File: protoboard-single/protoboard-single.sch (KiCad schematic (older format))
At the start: 1 part, among them J1 MODULE_HEADER

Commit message: mvp
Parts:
- added J10, J11, J12, J13, J14, J2, J3, J4, J5, J6, J7, J8, J9: MODULE_HEADER, parts:1x10, symbol MODULE_HEADER
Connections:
- net at J1.1 (GND): now also J14.1 (GND)
- net at J1.10 (G3): now also J14.10 (G3)
- net at J1.2 (3V3): now also J14.2 (3V3)
- net at J1.3 (SCL): now also J14.3 (SCL)
- net at J1.4 (SDA): now also J14.4 (SDA)
- net at J1.5 (CLK): now also J14.5 (CLK)
- net at J1.6 (MISO): now also J14.6 (MISO)
- net at J1.7 (MOSI): now also J14.7 (MOSI)
- net at J1.8 (G1/TX): now also J14.8 (G1/TX)
- net at J1.9 (G2/RX): now also J14.9 (G2/RX)
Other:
- note added: "cheating to get some through holes"
- moved on the sheet: J1
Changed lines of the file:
@@
 LIBS:valves
 LIBS:parts
-LIBS:protoboard-single-cache
 EELAYER 24 0
 EELAYER END
@@
 L MODULE_HEADER J1
 U 1 1 540E6C30
-P 5950 4000
-F 0 "J1" H 5600 4550 60  0000 C CNN
-F 1 "MODULE_HEADER" V 5650 3950 60  0000 C CNN
-F 2 "parts:MODULE_HEADER_MODULE" H 5950 4000 60  0001 C CNN
-F 3 "" H 5950 4000 60  0000 C CNN
-	1    5950 4000
+P 5400 2800
+F 0 "J1" H 5050 3350 60  0000 C CNN
+F 1 "MODULE_HEADER" V 5100 2750 60  0000 C CNN
+F 2 "parts:MODULE_HEADER_MODULE" H 5400 2800 60  0001 C CNN
+F 3 "" H 5400 2800 60  0000 C CNN
+	1    5400 2800
 	1    0    0    -1
 $EndComp
+$Comp
+L MODULE_HEADER J5
+U 1 1 540E71D1
+P 3450 5750
+F 0 "J5" H 3100 6300 60  0000 C CNN
+F 1 "MODULE_HEADER" V 3150 5700 60  0000 C CNN
+F 2 "parts:1x10" H 3450 5750 60  0001 C CNN
+F 3 "" H 3450 5750 60  0000 C CNN
+	1    3450 5750
+	1    0    0    -1
+$EndComp
+$Comp
+L MODULE_HEADER J6
+U 1 1 540E7221
+P 4300 5750
+F 0 "J6" H 3950 6300 60  0000 C CNN
+F 1 "MODULE_HEADER" V 4000 5700 60  0000 C CNN
+F 2 "parts:1x10" H 4300 5750 60  0001 C CNN
+F 3 "" H 4300 5750 60  0000 C CNN
+	1    4300 5750
+	1    0    0    -1
+$EndComp
+$Comp
+L MODULE_HEADER J7
+U 1 1 540E72AE
+P 5150 5750
+F 0 "J7" H 4800 6300 60  0000 C CNN
+F 1 "MODULE_HEADER" V 4850 5700 60  0000 C CNN
+F 2 "parts:1x10" H 5150 5750 60  0001 C CNN
+F 3 "" H 5150 5750 60  0000 C CNN
+	1    5150 5750
+	1    0    0    -1
+$EndComp
+$Comp
+L MODULE_HEADER J8
+U 1 1 540E72B4
+P 6000 5750
+F 0 "J8" H 5650 6300 60  0000 C CNN
+F 1 "MODULE_HEADER" V 5700 5700 60  0000 C CNN
+F 2 "parts:1x10" H 6000 5750 60  0001 C CNN
+F 3 "" H 6000 5750 60  0000 C CNN
+	1    6000 5750
+	1    0    0    -1
+$EndComp
+$Comp
+L MODULE_HEADER J9
+U 1 1 540E746F
+P 6850 5750
+F 0 "J9" H 6500 6300 60  0000 C CNN
+F 1 "MODULE_HEADER" V 6550 5700 60  0000 C CNN
+F 2 "parts:1x10" H 6850 5750 60  0001 C CNN
+F 3 "" H 6850 5750 60  0000 C CNN
+	1    6850 5750
+	1    0    0    -1
+$EndComp
+$Comp
+L MODULE_HEADER J10
+U 1 1 540E7475
+P 7700 5750
+F 0 "J10" H 7350 6300 60  0000 C CNN
+F 1 "MODULE_HEADER" V 7400 5700 60  0000 C CNN
+F 2 "parts:1x10" H 7700 5750 60  0001 C CNN
+F 3 "" H 7700 5750 60  0000 C CNN
+	1    7700 5750
+	1    0    0    -1
+$EndComp
+$Comp
+L MODULE_HEADER J11
+U 1 1 540E747B
+P 8550 5750
+F 0 "J11" H 8200 6300 60  0000 C CNN
+F 1 "MODULE_HEADER" V 8250 5700 60  0000 C CNN
+F 2 "parts:1x10" H 8550 5750 60  0001 C CNN
+F 3 "" H 8550 5750 60  0000 C CNN
+	1    8550 5750
+	1    0    0    -1
+$EndComp
+$Comp
+L MODULE_HEADER J12
+U 1 1 540E7481
+P 9400 5750
+F 0 "J12" H 9050 6300 60  0000 C CNN
+F 1 "MODULE_HEADER" V 9100 5700 60  0000 C CNN
+F 2 "parts:1x10" H 9400 5750 60  0001 C CNN
+F 3 "" H 9400 5750 60  0000 C CNN
+	1    9400 5750
+	1    0    0    -1
+$EndComp
+$Comp
+L MODULE_HEADER J2
+U 1 1 540E7CB6
+P 900 5750
+F 0 "J2" H 550 6300 60  0000 C CNN
+F 1 "MODULE_HEADER" V 600 5700 60  0000 C CNN
+F 2 "parts:1x10" H 900 5750 60  0001 C CNN
+F 3 "" H 900 5750 60  0000 C CNN
+	1    900  5750
+	1    0    0    -1
+$EndComp
+$Comp
+L MODULE_HEADER J3
+U 1 1 540E7CBC
+P 1750 5750
+F 0 "J3" H 1400 6300 60  0000 C CNN
+F 1 "MODULE_HEADER" V 1450 5700 60  0000 C CNN
+F 2 "parts:1x10" H 1750 5750 60  0001 C CNN
+F 3 "" H 1750 5750 60  0000 C CNN
+	1    1750 5750
+	1    0    0    -1
+$EndComp
+$Comp
+L MODULE_HEADER J4
+U 1 1 540E7CC2
+P 2600 5750
+F 0 "J4" H 2250 6300 60  0000 C CNN
+F 1 "MODULE_HEADER" V 2300 5700 60  0000 C CNN
+F 2 "parts:1x10" H 2600 5750 60  0001 C CNN
+F 3 "" H 2600 5750 60  0000 C CNN
+	1    2600 5750
+	1    0    0    -1
+$EndComp
+Text Notes 550  5000 0    60   ~ 0
+cheating to get some through holes
+$Comp
+L MODULE_HEADER J13
+U 1 1 540E81AD
+P 10200 5750
+F 0 "J13" H 9850 6300 60  0000 C CNN
+F 1 "MODULE_HEADER" V 9900 5700 60  0000 C CNN
+F 2 "parts:1x10" H 10200 5750 60  0001 C CNN
+F 3 "" H 10200 5750 60  0000 C CNN
+	1    10200 5750
+	1    0    0    -1
+$EndComp
+$Comp
+L MODULE_HEADER J14
+U 1 1 540E8463
+P 6200 2800
+F 0 "J14" H 5850 3350 60  0000 C CNN
+F 1 "MODULE_HEADER" V 5900 2750 60  0000 C CNN
+F 2 "parts:1x10" H 6200 2800 60  0001 C CNN
+F 3 "" H 6200 2800 60  0000 C CNN
+	1    6200 2800
+	-1   0    0    -1
+$EndComp
+Wire Wire Line
+	5900 2400 5700 2400
+Wire Wire Line
+	5700 2500 5900 2500
+Wire Wire Line
+	5900 2600 5700 2600
+Wire Wire Line
+	5700 2700 5900 2700
+Wire Wire Line
+	5900 2800 5700 2800
+Wire Wire Line
+	5700 2900 5900 2900
+Wire Wire Line
+	5900 3000 5700 3000
+Wire Wire Line
+	5700 3100 5900 3100
+Wire Wire Line
+	5900 3200 5700 3200
+Wire Wire Line
+	5700 3300 5900 3300
 $EndSCHEMATC

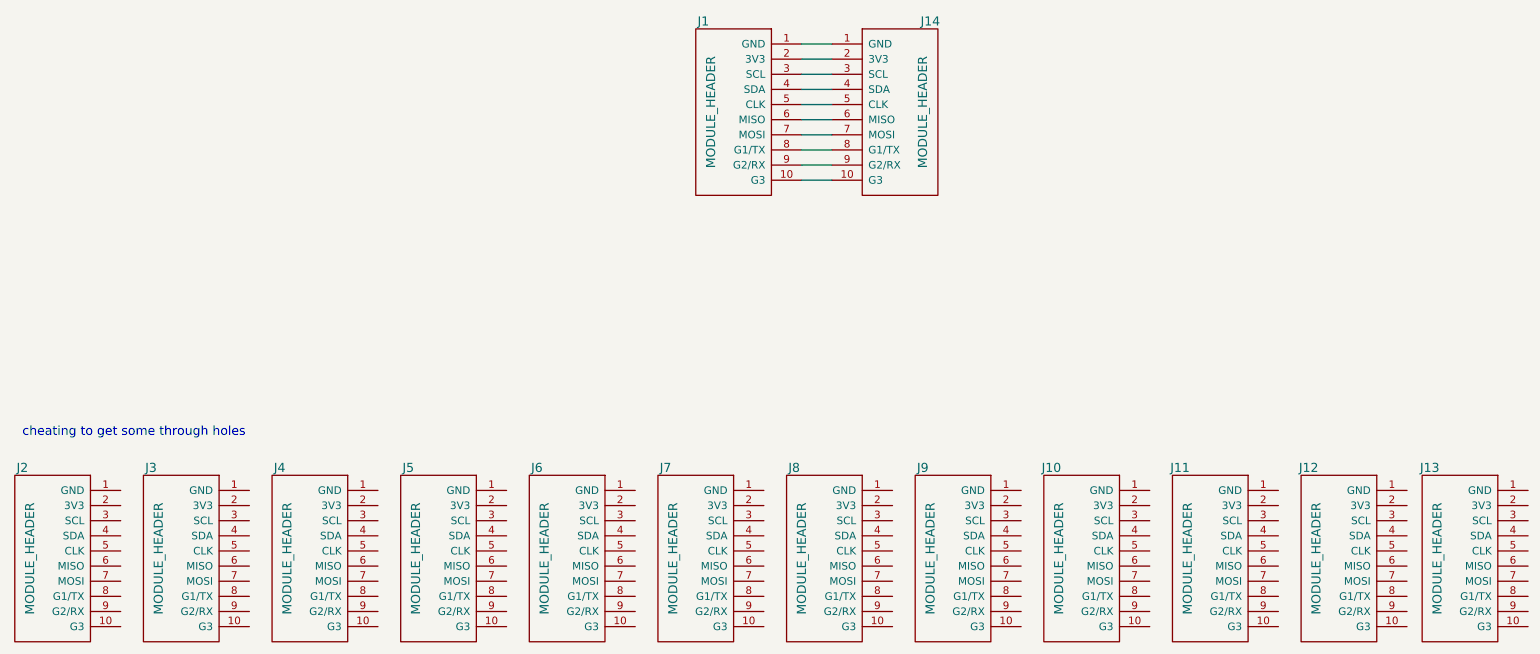
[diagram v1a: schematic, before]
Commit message: more access to each signal
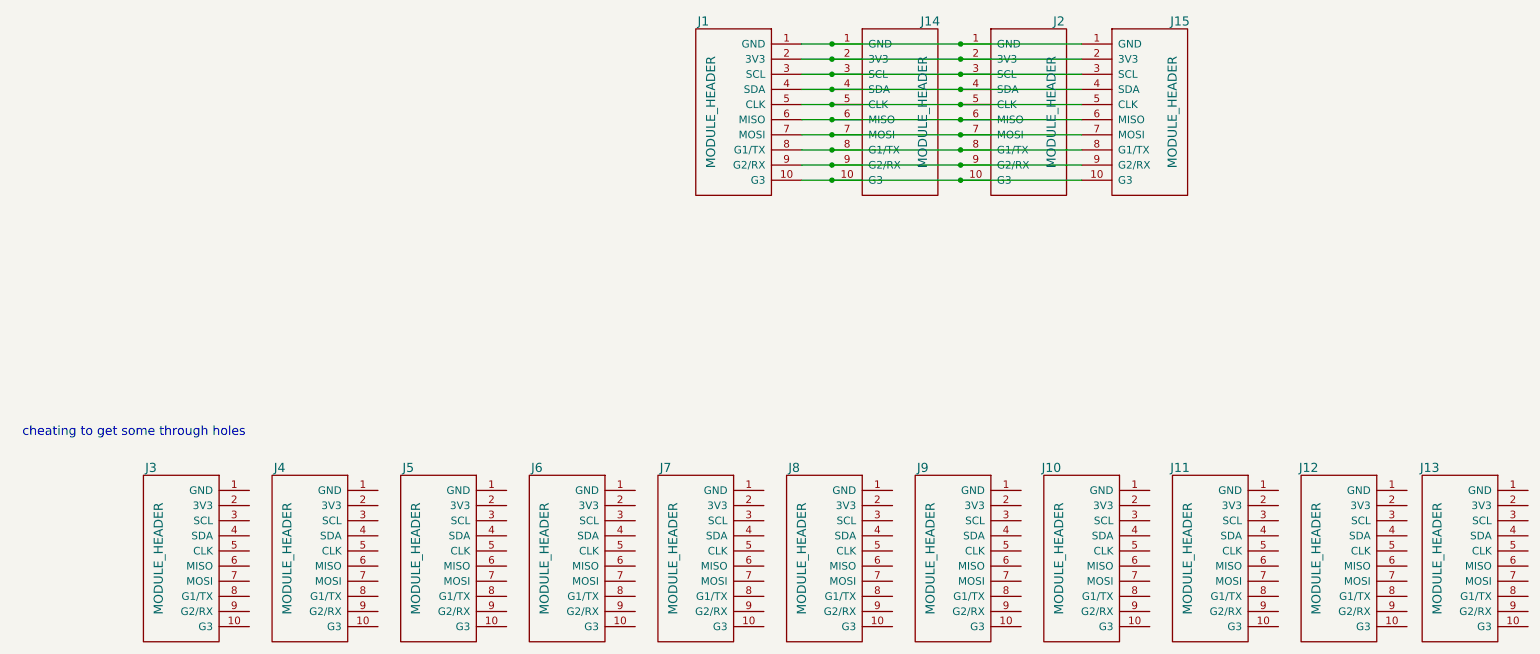
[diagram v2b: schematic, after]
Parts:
- added J15: MODULE_HEADER, parts:1x10, symbol MODULE_HEADER
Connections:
- net at J1.1 (GND), J14.1 (GND): now also J2.1 (GND), J15.1 (GND)
- net at J1.10 (G3), J14.10 (G3): now also J2.10 (G3), J15.10 (G3)
- net at J1.2 (3V3), J14.2 (3V3): now also J2.2 (3V3), J15.2 (3V3)
- net at J1.3 (SCL), J14.3 (SCL): now also J2.3 (SCL), J15.3 (SCL)
- net at J1.4 (SDA), J14.4 (SDA): now also J2.4 (SDA), J15.4 (SDA)
- net at J1.5 (CLK), J14.5 (CLK): now also J2.5 (CLK), J15.5 (CLK)
- net at J1.6 (MISO), J14.6 (MISO): now also J2.6 (MISO), J15.6 (MISO)
- net at J1.7 (MOSI), J14.7 (MOSI): now also J2.7 (MOSI), J15.7 (MOSI)
- net at J1.8 (G1/TX), J14.8 (G1/TX): now also J2.8 (G1/TX), J15.8 (G1/TX)
- net at J1.9 (G2/RX), J14.9 (G2/RX): now also J2.9 (G2/RX), J15.9 (G2/RX)
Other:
- moved on the sheet: J2
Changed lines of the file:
@@
 L MODULE_HEADER J2
 U 1 1 540E7CB6
-P 900 5750
-F 0 "J2" H 550 6300 60  0000 C CNN
-F 1 "MODULE_HEADER" V 600 5700 60  0000 C CNN
-F 2 "parts:1x10" H 900 5750 60  0001 C CNN
-F 3 "" H 900 5750 60  0000 C CNN
-	1    900  5750
-	1    0    0    -1
+P 7050 2800
+F 0 "J2" H 6700 3350 60  0000 C CNN
+F 1 "MODULE_HEADER" V 6750 2750 60  0000 C CNN
+F 2 "parts:1x10" H 7050 2800 60  0001 C CNN
+F 3 "" H 7050 2800 60  0000 C CNN
+	1    7050 2800
+	-1   0    0    -1
 $EndComp
 $Comp
@@
 $EndComp
 Wire Wire Line
-	5900 2400 5700 2400
+	5700 2400 7550 2400
 Wire Wire Line
-	5700 2500 5900 2500
+	5700 2500 7550 2500
 Wire Wire Line
-	5900 2600 5700 2600
+	5700 2600 7550 2600
 Wire Wire Line
-	5700 2700 5900 2700
+	5700 2700 7550 2700
 Wire Wire Line
-	5900 2800 5700 2800
+	5700 2800 7550 2800
 Wire Wire Line
-	5700 2900 5900 2900
+	5700 2900 7550 2900
 Wire Wire Line
-	5900 3000 5700 3000
+	5700 3000 7550 3000
 Wire Wire Line
-	5700 3100 5900 3100
+	5700 3100 7550 3100
 Wire Wire Line
-	5900 3200 5700 3200
+	5700 3200 7550 3200
 Wire Wire Line
-	5700 3300 5900 3300
+	5700 3300 7550 3300
+$Comp
+L MODULE_HEADER J15
+U 1 1 540E87DE
+P 7850 2800
+F 0 "J15" H 7500 3350 60  0000 C CNN
+F 1 "MODULE_HEADER" V 7550 2750 60  0000 C CNN
+F 2 "parts:1x10" H 7850 2800 60  0001 C CNN
+F 3 "" H 7850 2800 60  0000 C CNN
+	1    7850 2800
+	-1   0    0    -1
+$EndComp
+Connection ~ 5900 2400
+Connection ~ 5900 2500
+Connection ~ 5900 2600
+Connection ~ 5900 2700
+Connection ~ 5900 2800
+Connection ~ 5900 2900
+Connection ~ 5900 3000
+Connection ~ 5900 3100
+Connection ~ 5900 3200
+Connection ~ 5900 3300
+Connection ~ 6750 3300
+Connection ~ 6750 3200
+Connection ~ 6750 3100
+Connection ~ 6750 3000
+Connection ~ 6750 2900
+Connection ~ 6750 2800
+Connection ~ 6750 2700
+Connection ~ 6750 2600
+Connection ~ 6750 2500
+Connection ~ 6750 2400
 $EndSCHEMATC

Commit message: ship it
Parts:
- added SILK1: logo, parts:TESSEL-HEXAGON-LOGO, symbol logo
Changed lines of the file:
@@
 Connection ~ 6750 2500
 Connection ~ 6750 2400
+$Comp
+L logo SILK1
+U 1 1 540E8D3F
+P 3900 2800
+F 0 "SILK1" H 3900 2850 60  0000 C CNN
+F 1 "logo" H 3900 2750 60  0000 C CNN
+F 2 "parts:TESSEL-HEXAGON-LOGO" H 3900 2800 60  0001 C CNN
+F 3 "" H 3900 2800 60  0000 C CNN
+	1    3900 2800
+	1    0    0    -1
+$EndComp
 $EndSCHEMATC
